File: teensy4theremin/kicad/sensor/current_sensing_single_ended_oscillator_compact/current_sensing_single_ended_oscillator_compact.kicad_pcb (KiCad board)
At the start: 2 copper layers, 70.5 x 21.1 mm, 21 parts, among them J1 ANTENNA, J2 INDUCTOR_OUT, J3 INDUCTOR_IN, J6 OSC, U1 4220CZ6, U2 LD3985M33R_SOT23, U3 LT1711xMS8

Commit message: update pcb
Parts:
- added C13: 10nF, Capacitor_SMD:C_0805_2012Metric_Pad1.15x1.40mm_HandSolder, B.Cu at (142.2, 105.9)
- added C14: 1nF, Capacitor_SMD:C_0805_2012Metric_Pad1.15x1.40mm_HandSolder, B.Cu at (133.2, 105.8)
- added TP2: +3.3V, Connector_PinHeader_1.27mm:PinHeader_1x01_P1.27mm_Vertical, F.Cu at (130.4, 104.8)
- added TP3: GND, Connector_PinHeader_1.27mm:PinHeader_1x01_P1.27mm_Vertical, F.Cu at (130.4, 101.0)
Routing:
- net /3V3_A: track 30.0 -> 37.6 mm
- net GND: track 108.2 -> 109.8 mm
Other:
- board text added: "3.3V"
- board text added: "Current Sensing Theremin Oscillator rev 1.2 single ended output"
- board text removed: "Current Sensing Theremin Oscillator rev 1.2 single ended"

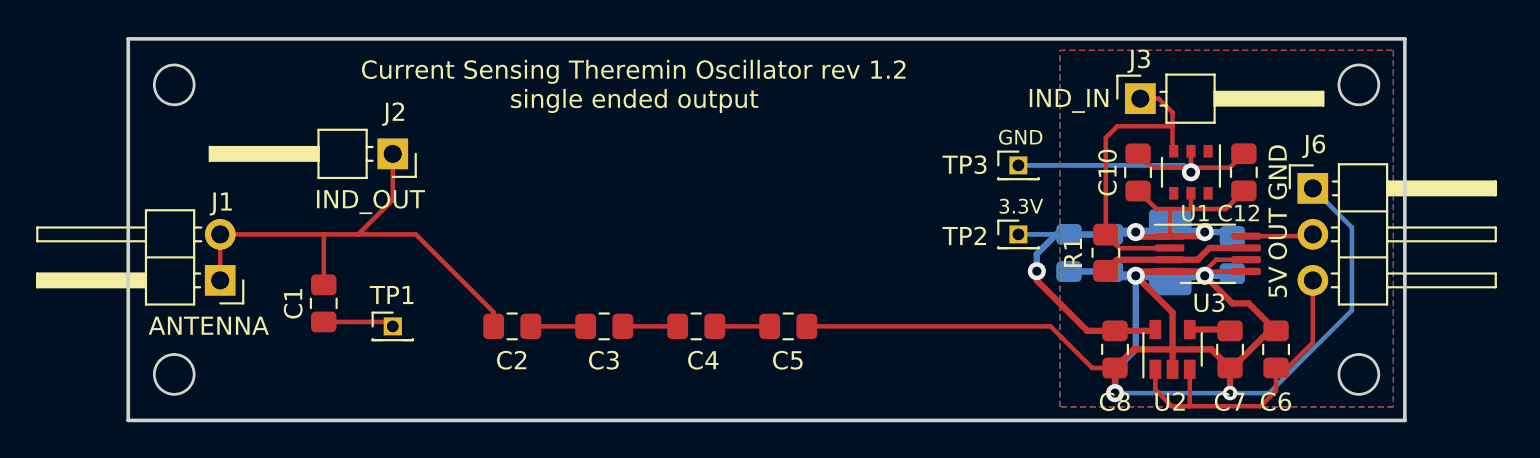
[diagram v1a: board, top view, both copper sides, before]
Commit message: update oscillator pcb
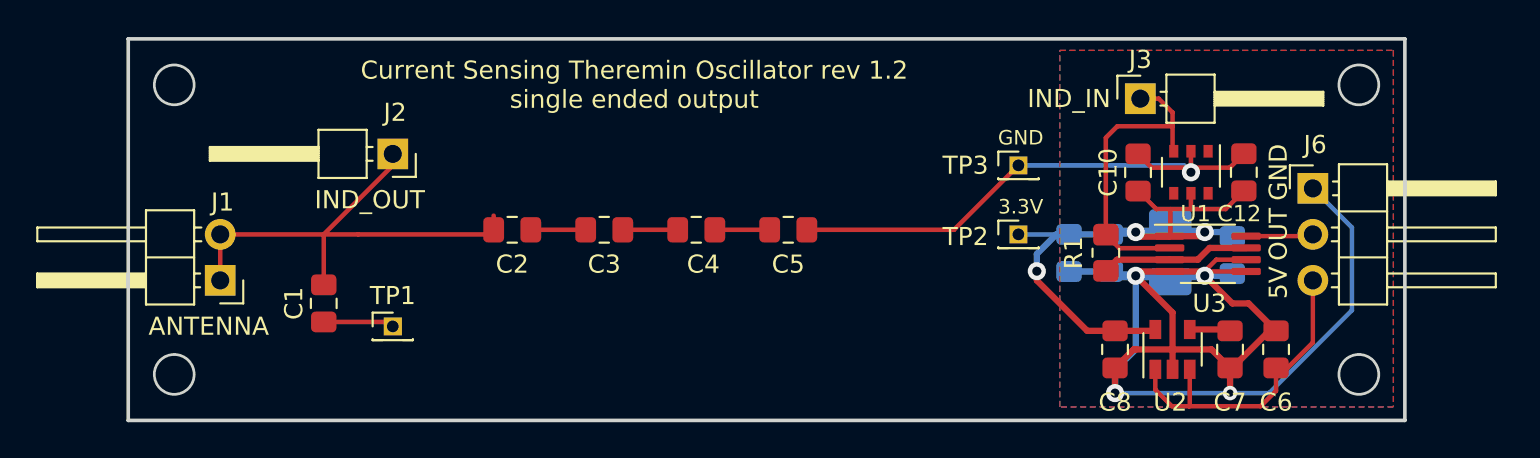
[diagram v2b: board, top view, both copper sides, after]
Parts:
- moved C2 5.33 mm to (102.5, 104.5)
- moved C3 5.33 mm to (107.6, 104.5)
- moved C4 5.33 mm to (112.6, 104.5)
- moved C5 5.33 mm to (117.7, 104.5)
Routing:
- net GND: track 109.8 -> 105.0 mm
- net Net-(C1-Pad2): track 28.2 -> 27.3 mm

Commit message: update sensor
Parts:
- added R2: 10, Resistor_SMD:R_0805_2012Metric_Pad1.20x1.40mm_HandSolder, F.Cu at (144.0, 101.3)
- added R3: 10, Resistor_SMD:R_0805_2012Metric_Pad1.20x1.40mm_HandSolder, F.Cu at (144.0, 105.4)
- added R4: 100, Resistor_SMD:R_0805_2012Metric_Pad1.20x1.40mm_HandSolder, B.Cu at (143.8, 108.7)
- added R5: 100, Resistor_SMD:R_0805_2012Metric_Pad1.20x1.40mm_HandSolder, B.Cu at (143.8, 100.8)
- C12, C8: value 1uF -> 2.2uF
- J6: footprint Connector_PinHeader_2.54mm:PinHeader_1x03_P2.54mm_Horizontal -> Connector_PinHeader_2.54mm:PinHeader_1x04_P2.54mm_Horizontal
- U2: value LD3985M33R_SOT23 -> LP2985AIM5-3.3
- U3: value LT1711xMS8 -> LT1711CMS8
- moved TP3 11.2 mm to (132.7, 111.9)
- moved C14 9.53 mm to (142.7, 105.4)
- moved TP2 5.11 mm to (132.7, 109.3)
- moved R1 2.00 mm to (133.6, 104.7)
- moved C10 1.61 mm to (135.5, 100.8), turned to 270 degrees
- moved C12 1.61 mm to (141.4, 100.8), turned to 270 degrees
- moved C13 1.61 mm to (140.7, 105.4)
- moved U1 1.61 mm to (138.4, 100.8), turned to 90 degrees
- moved C11 1.61 mm to (137.3, 105.3)
- moved U3 1.61 mm to (139.4, 105.3)
- moved C9 1.61 mm to (134.0, 105.3)
- moved J6 1.45 mm to (147.1, 100.8)
- moved C7 0.72 mm to (141.6, 110.6)
- moved C8 0.72 mm to (135.3, 110.6)
- moved C6 0.72 mm to (144.1, 110.6)
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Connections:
- J3 pad 1: Net-(J3-Pad1) -> /IND_IN
- J6 pad 2: /OUT_P -> /OUTP
- R1 pad 1: Net-(R1-Pad1) -> /DRIVE
- R1 pad 2: Net-(J3-Pad1) -> /IND_IN
- U1 pad 3: Net-(J3-Pad1) -> Net-(U1-Pad3)
- U1 pad 6: Net-(U1-Pad6) -> /IND_IN
- U3 pad 2: Net-(J3-Pad1) -> /IND_IN
- U3 pad 3: Net-(R1-Pad1) -> /DRIVE
- U3 pad 7: Net-(R1-Pad1) -> Net-(R2-Pad1)
- U3 pad 8: /OUT_P -> /DRIVE
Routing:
- net Net-(J3-Pad1): track 17.4 -> 0.00 mm
- net /IND_IN: track 0.00 -> 16.4 mm
- net /DRIVE: track 0.00 -> 11.0 mm
- net /OUTP: track 0.00 -> 9.14 mm
- net Net-(R1-Pad1): track 8.27 -> 0.00 mm
- net Net-(R2-Pad1): track 0.00 -> 7.27 mm
- net /OUTN: track 0.00 -> 6.30 mm
- net /OUT_P: track 3.72 -> 0.00 mm
- net /5V: track 17.9 -> 21.5 mm
- net /3V3_A: track 37.6 -> 40.9 mm
- net GND: track 105.0 -> 104.8 mm, vias 5 -> 4
- removed copper zone on F.Cu, net GND
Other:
- board text added: "+5V"
- board text added: "Current Sensing Theremin Oscillator rev 1.3 single ended or differential output"
- board text added: "N"
- board text added: "OUTN"
- board text added: "OUTP"
- board text added: "P"
- board text removed: "Current Sensing Theremin Oscillator rev 1.2 single ended output"
- board text removed: "OUT"
- board text removed: "V_IN"
